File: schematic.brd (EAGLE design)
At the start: 31.9 x 41.1 mm, 40 parts, among them CN1 1X4-BIG, CN2 1X4-BIG, IC3 78TO220, IC4 78TO220

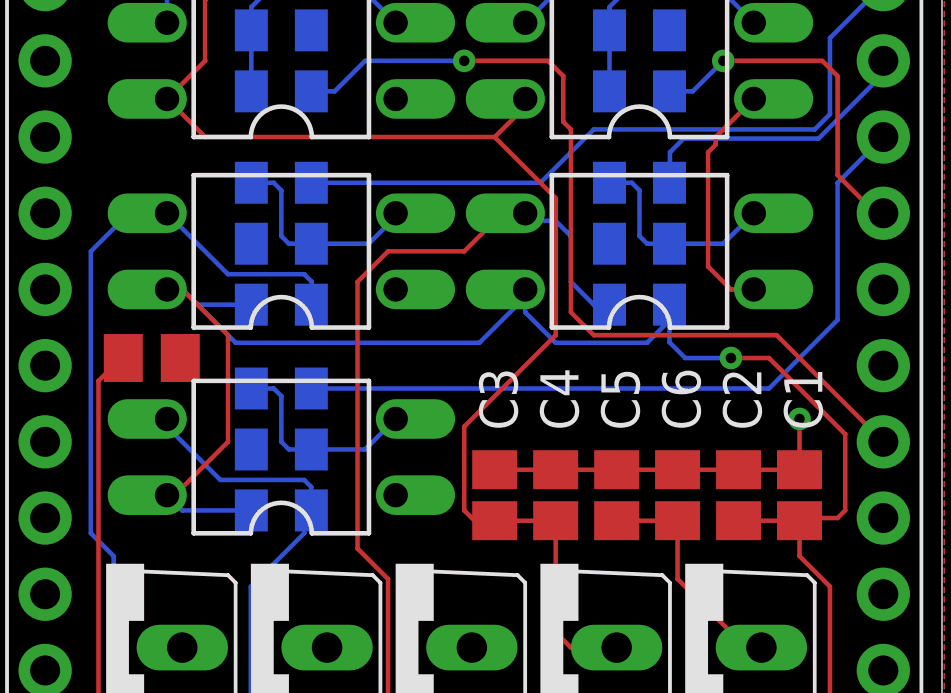
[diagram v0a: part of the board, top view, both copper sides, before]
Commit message: Inverted polarity of LED control on optocouplers
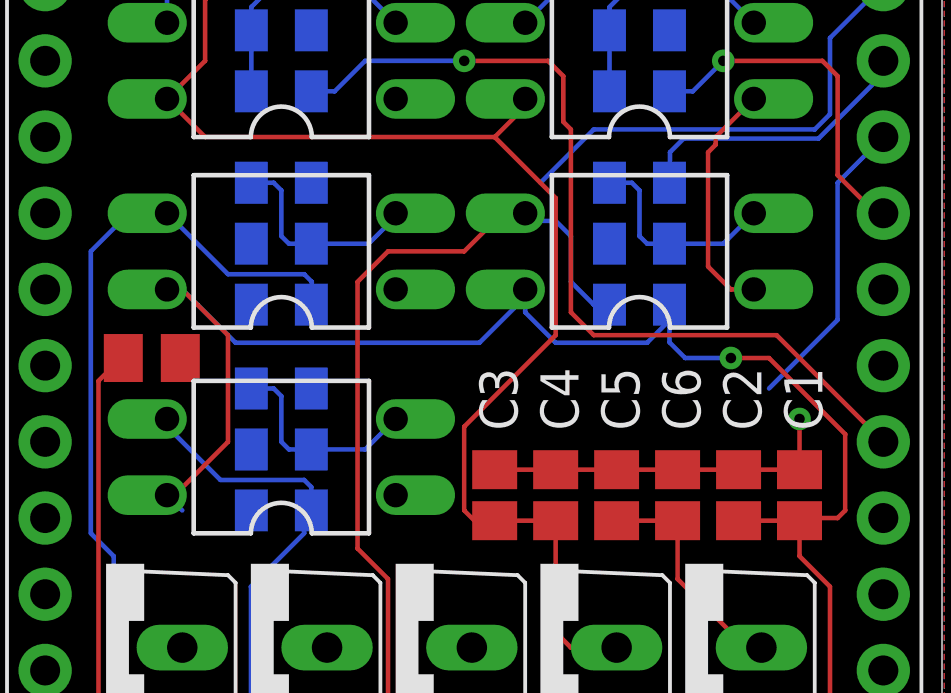
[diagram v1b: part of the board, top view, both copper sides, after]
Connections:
- net +12V: now also CN2.4; no longer R10.1, R8.1, R9.1
- net GND: now also R9.1; no longer CN2.4, R2.1, R3.1, R4.1
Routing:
- net CTRL_G: track 25.2 -> 9.96 mm
- net CTRL_B: track 23.3 -> 15.7 mm
- net +12V: track 77.9 -> 73.4 mm
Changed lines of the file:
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@@
 </element>
 <element name="R6" library="adafruit" package="R0805" value="" x="9.144" y="20.828" smashed="yes" rot="MR180">
-<attribute name="NAME" x="-5.08" y="23.368" size="1.27" layer="26" rot="MR180"/>
+<attribute name="NAME" x="-5.08" y="22.098" size="1.27" layer="26" rot="MR180"/>
 <attribute name="VALUE" x="8.382" y="23.114" size="1.27" layer="28" rot="MR180"/>
 </element>
@@
 <contactref element="C4" pad="2"/>
 <contactref element="CN1" pad="4"/>
-<contactref element="CN2" pad="4"/>
-<contactref element="R3" pad="1"/>
-<contactref element="R2" pad="1"/>
 <contactref element="Q1" pad="3"/>
 <contactref element="Q2" pad="3"/>
 <contactref element="Q3" pad="3"/>
-<contactref element="R4" pad="1"/>
 <contactref element="R11" pad="1"/>
 <contactref element="R12" pad="1"/>
@@
 <wire x1="26.416" y1="18.122" x2="26.416" y2="19.812" width="0.1524" layer="1"/>
 <via x="26.416" y="19.812" extent="1-16" drill="0.35"/>
+<contactref element="R9" pad="1"/>
+<wire x1="22.082" y1="32.766" x2="25.146" y2="35.322" width="0" layer="19" extent="16-16"/>
+<wire x1="18.796" y1="36.83" x2="22.082" y2="32.766" width="0" layer="19" extent="16-16"/>
+<wire x1="22.082" y1="23.622" x2="22.082" y2="32.766" width="0" layer="19" extent="16-16"/>
+<wire x1="22.352" y1="18.122" x2="22.082" y2="23.622" width="0" layer="19" extent="1-16"/>
+<wire x1="29.21" y1="21.59" x2="26.416" y2="19.812" width="0" layer="19" extent="1-1"/>
+<wire x1="15.494" y1="12.192" x2="16.256" y2="18.122" width="0" layer="19" extent="1-1"/>
+<wire x1="10.668" y1="12.192" x2="15.494" y2="12.192" width="0" layer="19" extent="1-1"/>
+<wire x1="5.842" y1="12.192" x2="10.668" y2="12.192" width="0" layer="19" extent="1-1"/>
+<wire x1="1.27" y1="13.97" x2="5.842" y2="12.192" width="0" layer="19" extent="1-1"/>
+<wire x1="20.32" y1="9.652" x2="15.494" y2="12.192" width="0" layer="19" extent="1-1"/>
+<wire x1="25.146" y1="9.652" x2="20.32" y2="9.652" width="0" layer="19" extent="1-1"/>
+<wire x1="23.688" y1="3.556" x2="25.146" y2="9.652" width="0" layer="19" extent="1-1"/>
+<wire x1="29.21" y1="3.81" x2="23.942" y2="3.302" width="0" layer="19" extent="1-1"/>
+<wire x1="1.27" y1="3.81" x2="5.842" y2="12.192" width="0" layer="19" extent="1-1"/>
+<wire x1="10.144" y1="32.766" x2="18.796" y2="36.83" width="0" layer="19" extent="16-16"/>
+<wire x1="6.858" y1="35.322" x2="10.144" y2="32.766" width="0" layer="19" extent="16-16"/>
+<wire x1="1.27" y1="34.29" x2="6.858" y2="35.322" width="0" layer="19" extent="16-16"/>
 </signal>
 <signal name="N$2">
@@
 <contactref element="C2" pad="1"/>
 <contactref element="LED1" pad="A"/>
-<contactref element="R10" pad="1"/>
-<contactref element="R8" pad="1"/>
-<contactref element="R9" pad="1"/>
 <contactref element="OK1" pad="4"/>
 <contactref element="OK2" pad="4"/>
@@
 <wire x1="5.588" y1="17.272" x2="7.366" y2="19.05" width="0.1524" layer="1"/>
 <wire x1="7.366" y1="19.05" x2="7.366" y2="22.606" width="0.1524" layer="1"/>
-<wire x1="8.144" y1="16.764" x2="5.842" y2="16.764" width="0.1524" layer="16"/>
 <wire x1="5.842" y1="16.764" x2="5.334" y2="17.272" width="0.1524" layer="16"/>
 <wire x1="15.748" y1="22.352" x2="7.62" y2="22.352" width="0.1524" layer="16"/>
@@
 <wire x1="5.842" y1="24.13" x2="5.334" y2="24.13" width="0.1524" layer="16"/>
 <wire x1="17.272" y1="23.876" x2="15.748" y2="22.352" width="0.1524" layer="16"/>
-<wire x1="8.144" y1="23.622" x2="6.35" y2="23.622" width="0.1524" layer="16"/>
 <wire x1="6.35" y1="23.622" x2="5.842" y2="24.13" width="0.1524" layer="16"/>
 <wire x1="26.416" y1="16.422" x2="26.504" y2="16.51" width="0.1524" layer="1"/>
@@
 <wire x1="17.78" y1="1.27" x2="17.78" y2="1.778" width="0.1524" layer="1"/>
 <wire x1="22.708" y1="0.508" x2="18.542" y2="0.508" width="0.1524" layer="1"/>
-<wire x1="22.082" y1="23.183809375" x2="22.082" y2="23.622" width="0.1524" layer="16"/>
 <wire x1="22.082" y1="23.183809375" x2="22.082" y2="22.368" width="0.1524" layer="16"/>
 <wire x1="17.272" y1="23.368" x2="18.288" y2="22.352" width="0.1524" layer="16"/>
@@
 <wire x1="21.336" y1="22.352" x2="22.082" y2="23.098" width="0.1524" layer="16"/>
 <wire x1="22.082" y1="23.098" x2="22.082" y2="23.183809375" width="0.1524" layer="16"/>
+<contactref element="CN2" pad="4"/>
+<wire x1="12.7" y1="1.778" x2="17.78" y2="1.778" width="0" layer="19" extent="16-16"/>
 </signal>
 <signal name="CTRL_A_5V">
@@
 </signal>
 <signal name="CTRL_R">
-<contactref element="R7" pad="2"/>
 <contactref element="U$1" pad="P$28"/>
 <wire x1="29.21" y1="31.75" x2="29.21" y2="31.31894375" width="0.1524" layer="16"/>
 <wire x1="27.05025625" y1="29.1592" x2="22.5552" y2="29.1592" width="0.1524" layer="16"/>
 <wire x1="22.098" y1="28.702" x2="22.098" y2="27.702" width="0.1524" layer="16"/>
-<wire x1="22.098" y1="27.702" x2="22.082" y2="27.686" width="0.1524" layer="16"/>
 <wire x1="29.21" y1="31.31894375" x2="27.05025625" y2="29.1592" width="0.1524" layer="16"/>
 <wire x1="22.5552" y1="29.1592" x2="22.098" y2="28.702" width="0.1524" layer="16"/>
+<contactref element="R7" pad="2"/>
+<wire x1="22.082" y1="27.686" x2="22.098" y2="27.702" width="0" layer="19" extent="16-16"/>
 </signal>
 <signal name="CTRL_G">
-<contactref element="R6" pad="2"/>
-<wire x1="10.144" y1="20.828" x2="25.4" y2="20.828" width="0.1524" layer="16"/>
 <wire x1="25.4" y1="20.828" x2="27.686" y2="23.114" width="0.1524" layer="16"/>
 <contactref element="U$1" pad="P$27"/>
 <wire x1="27.686" y1="23.114" x2="27.686" y2="27.686" width="0.1524" layer="16"/>
 <wire x1="27.686" y1="27.686" x2="29.21" y2="29.21" width="0.1524" layer="16"/>
+<contactref element="R6" pad="2"/>
+<wire x1="10.144" y1="20.828" x2="25.4" y2="20.828" width="0" layer="19" extent="16-16"/>
 </signal>
 <signal name="CTRL_B">
-<contactref element="R5" pad="2"/>
 <contactref element="U$1" pad="P$29"/>
-<wire x1="10.144" y1="27.686" x2="17.78" y2="27.686" width="0.1524" layer="16"/>
 <wire x1="19.558" y1="29.464" x2="26.924" y2="29.464" width="0.1524" layer="16"/>
 <wire x1="26.924" y1="29.464" x2="27.432" y2="29.972" width="0.1524" layer="16"/>
@@
 <wire x1="27.432" y1="32.512" x2="29.21" y2="34.29" width="0.1524" layer="16"/>
 <wire x1="17.78" y1="27.686" x2="19.558" y2="29.464" width="0.1524" layer="16"/>
+<contactref element="R5" pad="2"/>
+<wire x1="10.144" y1="27.686" x2="17.78" y2="27.686" width="0" layer="19" extent="16-16"/>
 </signal>
 <signal name="CTRL_A_3V3">

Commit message: Updated board; enhanced schematics organization
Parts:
- R1, R13, R14, R15, R16, R19, R5, R6, R7: value (none) -> 1k
- R10, R11, R12, R17, R18, R2, R3, R4, R8, R9: value (none) -> 10k
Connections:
- net +3V3: now also R2.1, R3.1, R4.1
- net GND: now also R10.1, R8.1
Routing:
- net +3V3: track 15.8 -> 32.1 mm
- net CTRL_G: track 9.96 -> 25.4 mm
- net CTRL_B: track 15.7 -> 23.3 mm
- net +12V: track 73.4 -> 77.1 mm
- net GND: track 16.3 -> 17.8 mm, vias 1 -> 3
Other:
- board text added: "v1.1"
- board text removed: "v1.0"
